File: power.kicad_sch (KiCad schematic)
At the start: 0 parts

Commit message: more esc schematics, refactoring, root schematic edits
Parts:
- added C17, C19: 100nF, Capacitor_SMD:C_0603_1608Metric_Pad1.08x0.95mm_HandSolder, symbol Device:C_Small
- added C18, C20: 10uF, Capacitor_SMD:C_0603_1608Metric_Pad1.08x0.95mm_HandSolder, symbol Device:C_Small
- added U4: MCP1826S, Package_TO_SOT_SMD:SOT-223-3_TabPin2, symbol Regulator_Linear:MCP1826S
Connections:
- new net +3V3: C19.1, C20.2, U4.3 (VO)
- new net GND_BK_M1: C17.2, C18.1, C19.2, C20.1, U4.2 (GND)
- new net VBK_M1: C17.1, C18.2, U4.1 (VI)

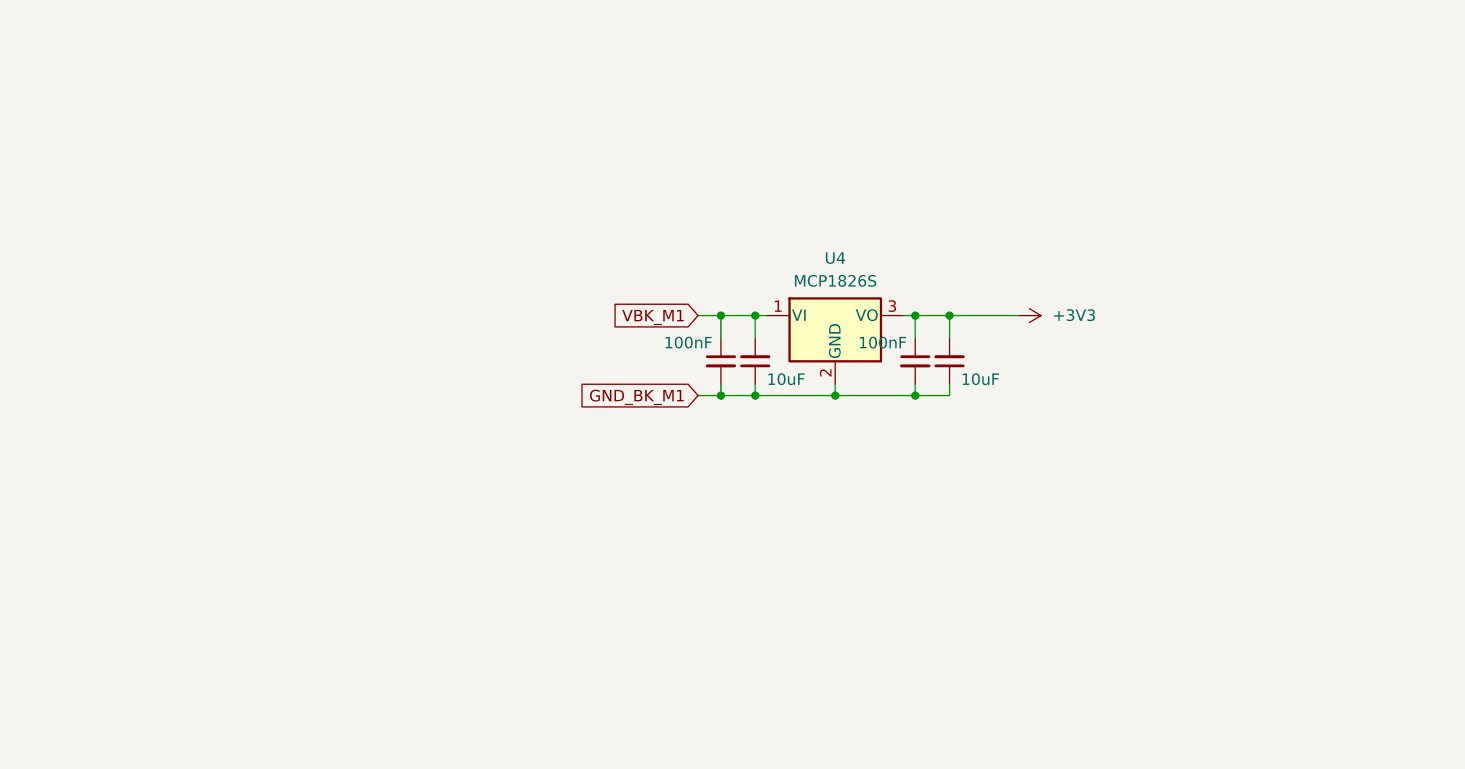
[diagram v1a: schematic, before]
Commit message: A LOT of changes, current state is 2 of 4 ESCs routed, power revamped. \n Board almost done
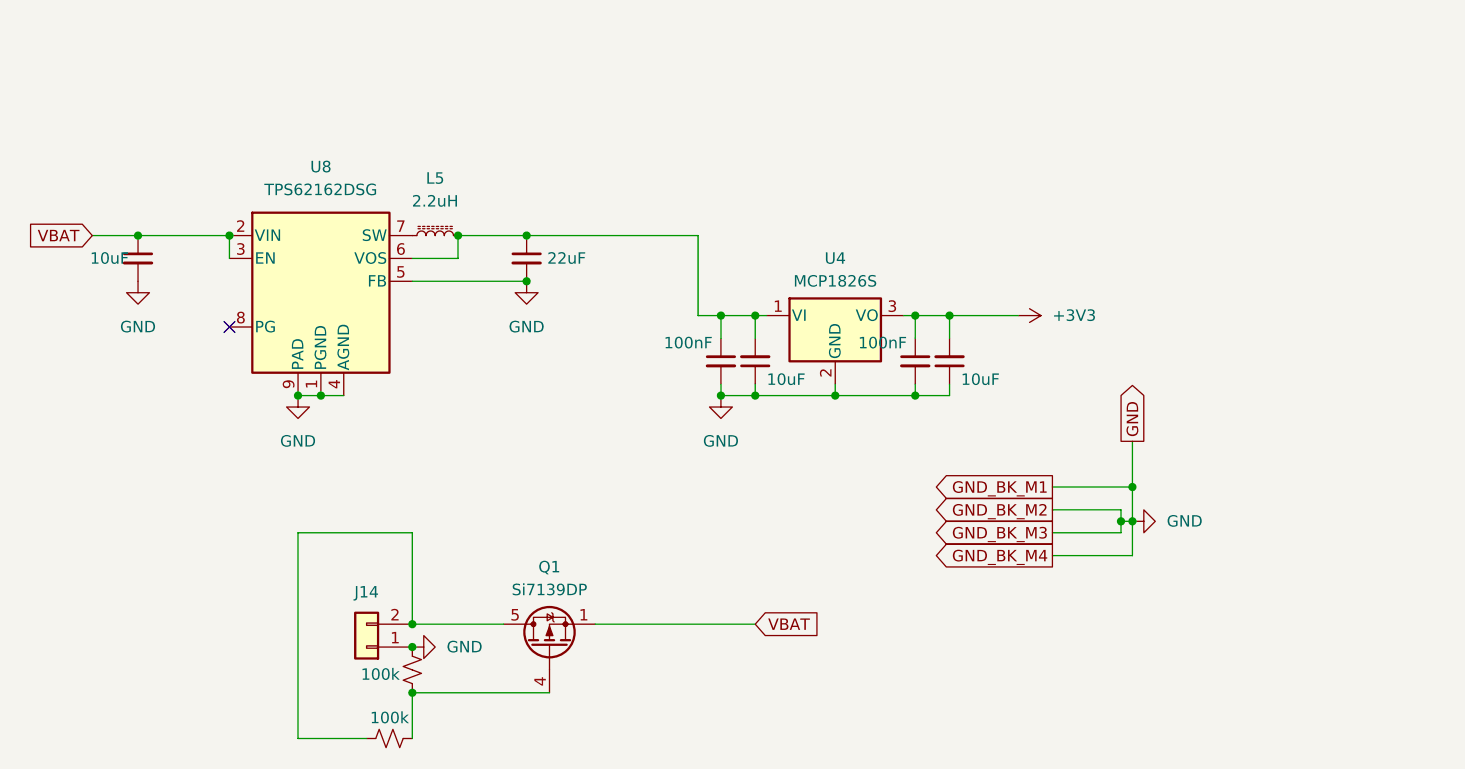
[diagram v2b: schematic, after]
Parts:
- added C42: 10uF, Capacitor_SMD:C_0603_1608Metric_Pad1.08x0.95mm_HandSolder, symbol Device:C_Small
- added C43: 22uF, Capacitor_SMD:C_1206_3216Metric_Pad1.33x1.80mm_HandSolder, symbol Device:C_Small
- added J14: Conn_01x02, Connector_Wire:SolderWire-2sqmm_1x02_P7.8mm_D2mm_OD3.9mm, symbol Connector_Generic:Conn_01x02
- added L5: 2.2uH, Inductor_SMD:L_1008_2520Metric_Pad1.43x2.20mm_HandSolder, symbol Device:L_Ferrite_Small
- added Q1: Si7139DP, Package_SO:PowerPAK_SO-8_Single, symbol Transistor_FET:Si7141DP
- added R16, R17: 100k, Resistor_SMD:R_0603_1608Metric_Pad0.98x0.95mm_HandSolder, symbol Device:R_Small_US
- added U8: TPS62162DSG, Package_SON:WSON-8-1EP_2x2mm_P0.5mm_EP0.9x1.6mm, symbol Regulator_Switching:TPS62163DSG
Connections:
- net GND_BK_M1 renamed GND
- net GND: now also C42.2, C43.2, J14.1 (Pin_1), R17.2, U8.1 (PGND), U8.4 (AGND), U8.5 (FB), U8.9 (PAD)
- net VBK_M1: no longer names the net of C17.1, C18.2, U4.1 (VI)
- net VBK_M1: now also C43.1, L5.2, U8.6 (VOS)
- new net: L5.1, U8.7 (SW)
- new net: J14.2 (Pin_2), Q1.5 (D), R16.1
- new net: Q1.4 (G), R16.2, R17.1
- new net VBAT: C42.1, Q1.1 (S), Q1.2 (S), Q1.3 (S), U8.2 (VIN), U8.3 (EN)
- no-connect marks 0 -> 1

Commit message: done?
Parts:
- removed R16: 100k, Resistor_SMD:R_0603_1608Metric_Pad0.98x0.95mm_HandSolder, symbol Device:R_Small_US
- added C9: 330uF, Capacitor_SMD:CP_Elec_10x10.5, symbol Device:C_Polarized_Small
- added D1: BZT52H-B12, Diode_SMD:D_SOD-123, symbol Device:D_Zener_Small
- added D2: SMAJ18A, Diode_SMD:D_SMA_Handsoldering, symbol Diode:SMAJ18A
- added D3: LED_Small, LED_SMD:LED_0402_1005Metric_Pad0.77x0.64mm_HandSolder, symbol Device:LED_Small
- added R6: 220, Resistor_SMD:R_0402_1005Metric_Pad0.72x0.64mm_HandSolder, symbol Device:R_Small_US
- R17: footprint Resistor_SMD:R_0603_1608Metric_Pad0.98x0.95mm_HandSolder -> Resistor_SMD:R_0402_1005Metric_Pad0.72x0.64mm_HandSolder
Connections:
- net +3V3: now also D3.2 (A)
- net GND: now also C9.2, D2.1 (A1), R6.2
- net VBAT: now also C9.1, D1.1 (K), D2.2 (A2)
- net +5V: now reaches C17.1, C18.2, C43.1, L5.2, U4.1 (VI), U8.6 (VOS)
- net at Q1.4 (G), R17.1: now also D1.2 (A)
- new net: D3.1 (K), R6.1
